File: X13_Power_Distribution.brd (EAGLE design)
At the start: 152.4 x 73.7 mm, 43 parts, among them Q1 310mA/60V/1.6Ω, U1 Value, U2 Value

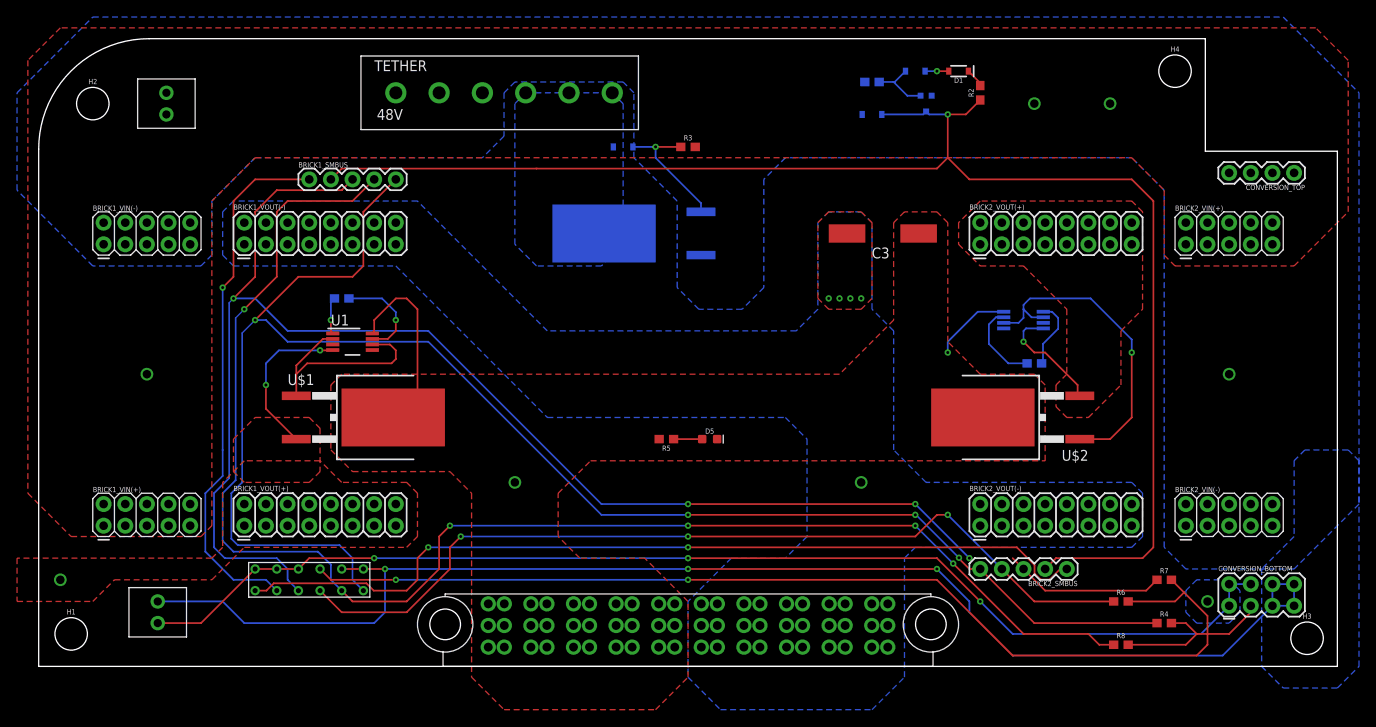
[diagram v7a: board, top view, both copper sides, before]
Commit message: Routed with custom connectors
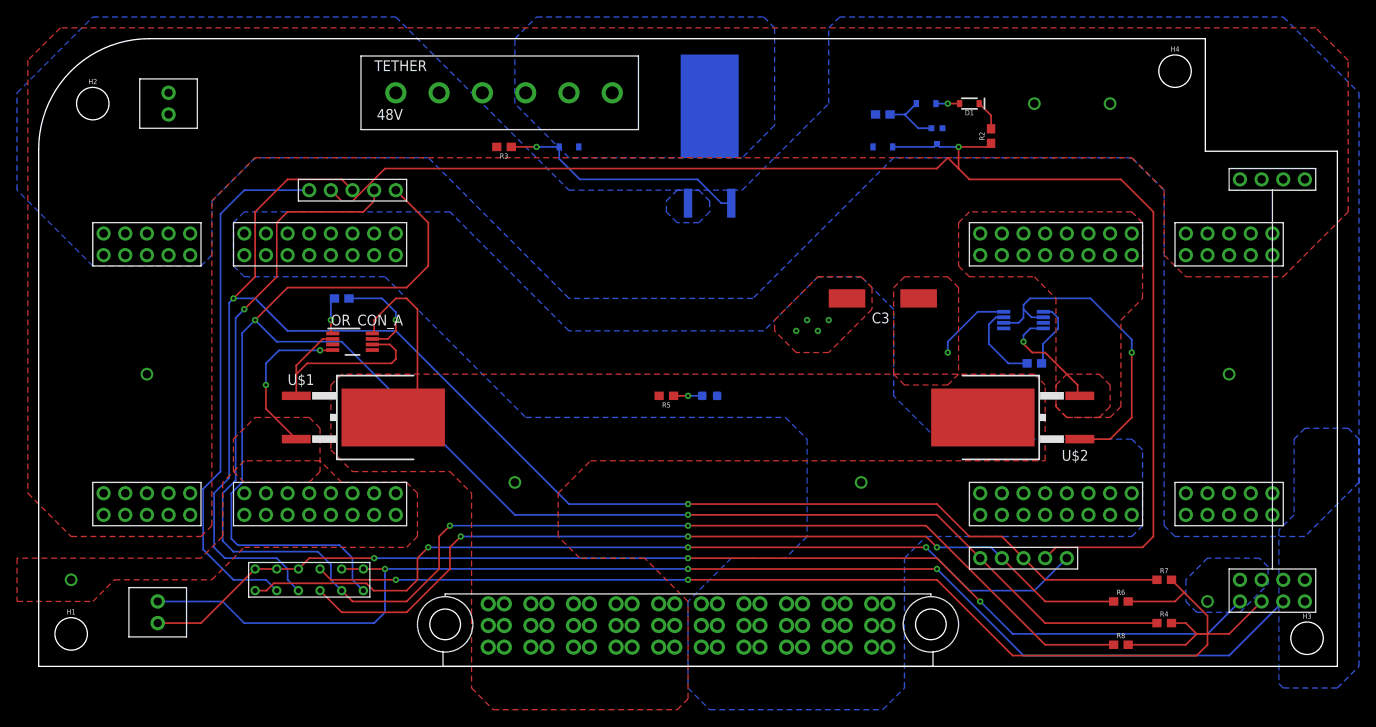
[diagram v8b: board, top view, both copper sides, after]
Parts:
- removed BRICK1_SMBUS, BRICK2_SMBUS: (no value), SparkFun-Connectors:1X05
- removed BRICK1_VIN(+), BRICK1_VIN(-), BRICK2_VIN(+), BRICK2_VIN(-): (no value), SparkFun-Connectors:2X5
- removed BRICK1_VOUT(+), BRICK1_VOUT(-), BRICK2_VOUT(+), BRICK2_VOUT(-): (no value), SparkFun-Connectors:2X8
- removed CONVERSION_BOTTOM: (no value), SparkFun-Connectors:2X4
- removed CONVERSION_TOP: (no value), SparkFun-Connectors:1X04
- added CONVERSION: DIST2CON, Dist_Convert_Connector:DIST2CON
- added U$3, U$4: (no value), Brick_Dist_Connector:DIST2BRICK
- moved R3 21.6 mm to (54.6, 61.0), turned to 180 degrees
- moved U$6 12.7 mm to (78.7, 61.0), turned to 0 degrees
- moved C3 7.62 mm to (99.1, 43.2)
- moved D6 6.35 mm to (62.2, 61.0), turned to 180 degrees
- moved R2 5.24 mm to (111.8, 62.2)
- moved D5 5.08 mm to (78.7, 31.8), flipped to the bottom, turned to 180 degrees
- moved R5 5.08 mm to (73.7, 31.8)
- moved Q1 4.02 mm to (105.4, 62.2)
- moved R1 4.02 mm to (99.1, 64.8)
- moved D2 4.02 mm to (99.1, 61.0)
- moved D1 4.02 mm to (109.2, 66.0)
- moved D3 4.02 mm to (104.1, 66.0)
- moved 48V_POE 0.25 mm to (15.2, 64.8)
- renumbered J1 to BACKPLANE_PWR, U1 to OR_CON_A, U2 to OR_CON_B
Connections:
- net N$10 renamed OR_DRIVE_A
- net N$13 renamed OR_DRIVE_B
- net N$2 renamed ON/OFF_DRIVE
- net N$3 renamed REV_DRIVE
- net N$5 renamed VCAPH_B
- net N$6 renamed VCAPL_B
- net N$7 renamed VCAPL_A
- net N$9 renamed VCAPH_A
- removed net GND: D5.C
- net +12V_A: now also U$3.2@1, U$3.2@10, U$3.2@11, U$3.2@12, U$3.2@13, U$3.2@14, U$3.2@15, U$3.2@16, U$3.2@2, U$3.2@3, U$3.2@4, U$3.2@5, U$3.2@6, U$3.2@7, U$3.2@8, U$3.2@9; no longer BRICK1_VOUT(+).1, BRICK1_VOUT(+).10, BRICK1_VOUT(+).11, BRICK1_VOUT(+).12, BRICK1_VOUT(+).13, BRICK1_VOUT(+).14, BRICK1_VOUT(+).15, BRICK1_VOUT(+).16, BRICK1_VOUT(+).2, BRICK1_VOUT(+).3, BRICK1_VOUT(+).4, BRICK1_VOUT(+).5, BRICK1_VOUT(+).6, BRICK1_VOUT(+).7, BRICK1_VOUT(+).8, BRICK1_VOUT(+).9
- net +12V_B: now also U$4.2@1, U$4.2@10, U$4.2@11, U$4.2@12, U$4.2@13, U$4.2@14, U$4.2@15, U$4.2@16, U$4.2@2, U$4.2@3, U$4.2@4, U$4.2@5, U$4.2@6, U$4.2@7, U$4.2@8, U$4.2@9; no longer BRICK2_VOUT(+).1, BRICK2_VOUT(+).10, BRICK2_VOUT(+).11, BRICK2_VOUT(+).12, BRICK2_VOUT(+).13, BRICK2_VOUT(+).14, BRICK2_VOUT(+).15, BRICK2_VOUT(+).16, BRICK2_VOUT(+).2, BRICK2_VOUT(+).3, BRICK2_VOUT(+).4, BRICK2_VOUT(+).5, BRICK2_VOUT(+).6, BRICK2_VOUT(+).7, BRICK2_VOUT(+).8, BRICK2_VOUT(+).9
- net +3.3V: now also CONVERSION.4; no longer CONVERSION_BOTTOM.3
- net +48V: now also CONVERSION.1@1, CONVERSION.1@2, U$3.1@1, U$3.1@10, U$3.1@2, U$3.1@3, U$3.1@4, U$3.1@5, U$3.1@6, U$3.1@7, U$3.1@8, U$3.1@9, U$4.1@1, U$4.1@10, U$4.1@2, U$4.1@3, U$4.1@4, U$4.1@5, U$4.1@6, U$4.1@7, U$4.1@8, U$4.1@9; no longer BRICK1_VIN(+).1, BRICK1_VIN(+).10, BRICK1_VIN(+).2, BRICK1_VIN(+).3, BRICK1_VIN(+).4, BRICK1_VIN(+).5, BRICK1_VIN(+).6, BRICK1_VIN(+).7, BRICK1_VIN(+).8, BRICK1_VIN(+).9, BRICK2_VIN(+).1, BRICK2_VIN(+).10, BRICK2_VIN(+).2, BRICK2_VIN(+).3, BRICK2_VIN(+).4, BRICK2_VIN(+).5, BRICK2_VIN(+).6, BRICK2_VIN(+).7, BRICK2_VIN(+).8, BRICK2_VIN(+).9, CONVERSION_TOP.3, CONVERSION_TOP.4
- net +5V: now also CONVERSION.3@1, CONVERSION.3@2, CONVERSION.3@3; no longer CONVERSION_BOTTOM.1, CONVERSION_BOTTOM.2, CONVERSION_BOTTOM.4
- net 12V_GND: now also D5.C, U$3.4@1, U$3.4@10, U$3.4@11, U$3.4@12, U$3.4@13, U$3.4@14, U$3.4@15, U$3.4@16, U$3.4@2, U$3.4@3, U$3.4@4, U$3.4@5, U$3.4@6, U$3.4@7, U$3.4@8, U$3.4@9, U$4.4@1, U$4.4@10, U$4.4@11, U$4.4@12, U$4.4@13, U$4.4@14, U$4.4@15, U$4.4@16, U$4.4@2, U$4.4@3, U$4.4@4, U$4.4@5, U$4.4@6, U$4.4@7, U$4.4@8, U$4.4@9; no longer BRICK1_VOUT(-).1, BRICK1_VOUT(-).10, BRICK1_VOUT(-).11, BRICK1_VOUT(-).12, BRICK1_VOUT(-).13, BRICK1_VOUT(-).14, BRICK1_VOUT(-).15, BRICK1_VOUT(-).16, BRICK1_VOUT(-).2, BRICK1_VOUT(-).3, BRICK1_VOUT(-).4, BRICK1_VOUT(-).5, BRICK1_VOUT(-).6, BRICK1_VOUT(-).7, BRICK1_VOUT(-).8, BRICK1_VOUT(-).9, BRICK2_VOUT(-).1, BRICK2_VOUT(-).10, BRICK2_VOUT(-).11, BRICK2_VOUT(-).12, BRICK2_VOUT(-).13, BRICK2_VOUT(-).14, BRICK2_VOUT(-).15, BRICK2_VOUT(-).16, BRICK2_VOUT(-).2, BRICK2_VOUT(-).3, BRICK2_VOUT(-).4, BRICK2_VOUT(-).5, BRICK2_VOUT(-).6, BRICK2_VOUT(-).7, BRICK2_VOUT(-).8, BRICK2_VOUT(-).9
- net 48V_GND: now also CONVERSION.2@1, CONVERSION.2@2, U$3.3@1, U$3.3@10, U$3.3@2, U$3.3@3, U$3.3@4, U$3.3@5, U$3.3@6, U$3.3@7, U$3.3@8, U$3.3@9, U$4.3@1, U$4.3@10, U$4.3@2, U$4.3@3, U$4.3@4, U$4.3@5, U$4.3@6, U$4.3@7, U$4.3@8, U$4.3@9; no longer BRICK1_VIN(-).1, BRICK1_VIN(-).10, BRICK1_VIN(-).2, BRICK1_VIN(-).3, BRICK1_VIN(-).4, BRICK1_VIN(-).5, BRICK1_VIN(-).6, BRICK1_VIN(-).7, BRICK1_VIN(-).8, BRICK1_VIN(-).9, BRICK2_VIN(-).1, BRICK2_VIN(-).10, BRICK2_VIN(-).2, BRICK2_VIN(-).3, BRICK2_VIN(-).4, BRICK2_VIN(-).5, BRICK2_VIN(-).6, BRICK2_VIN(-).7, BRICK2_VIN(-).8, BRICK2_VIN(-).9, CONVERSION_TOP.1, CONVERSION_TOP.2
- net 5V_GND: now also CONVERSION.5@1, CONVERSION.5@2, CONVERSION.5@3, CONVERSION.5@4; no longer CONVERSION_BOTTOM.5, CONVERSION_BOTTOM.6, CONVERSION_BOTTOM.7, CONVERSION_BOTTOM.8
- net ALERT_1: now also U$3.D; no longer BRICK1_SMBUS.4
- net ALERT_2: now also U$4.D; no longer BRICK2_SMBUS.4
- net C2_1: now also U$3.A; no longer BRICK1_SMBUS.1
- net C2_2: now also U$4.A; no longer BRICK2_SMBUS.1
- net CLK: now also U$3.C, U$4.C; no longer BRICK1_SMBUS.3, BRICK2_SMBUS.3
- net DATA: now also U$3.E, U$4.E; no longer BRICK1_SMBUS.5, BRICK2_SMBUS.5
- net ON/OFF: now also U$3.B, U$4.B; no longer BRICK1_SMBUS.2, BRICK2_SMBUS.2
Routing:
- net REV_DRIVE: track 15.4 -> 29.4 mm
- net 5V_GND: track 160.1 -> 150.7 mm
- net DATA: track 194.0 -> 200.3 mm, vias 4 -> 2
- net CLK: track 185.2 -> 189.7 mm, vias 4 -> 2
- net +5V: track 139.0 -> 135.4 mm
- net ON/OFF: track 171.7 -> 168.2 mm
- net ALERT_2: track 104.6 -> 102.5 mm
- net +48V: track 2.27 -> 3.54 mm
- net +3.3V: track 145.8 -> 146.8 mm
- net C2_2: track 102.2 -> 103.2 mm, vias 2 -> 3
- net ALERT_1: track 174.5 -> 174.0 mm, vias 5 -> 3
- net C2_1: track 62.7 -> 62.4 mm, vias 1 -> 0
- net N$8: vias 0 -> 1
